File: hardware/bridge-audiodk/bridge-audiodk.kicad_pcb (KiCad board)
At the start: 6 copper layers, 5 parts, among them J1 Conn_01x08_Pin, J2 Conn_01x06_Pin, J3 Conn_01x08_Pin, J4 Conn_01x08_Pin

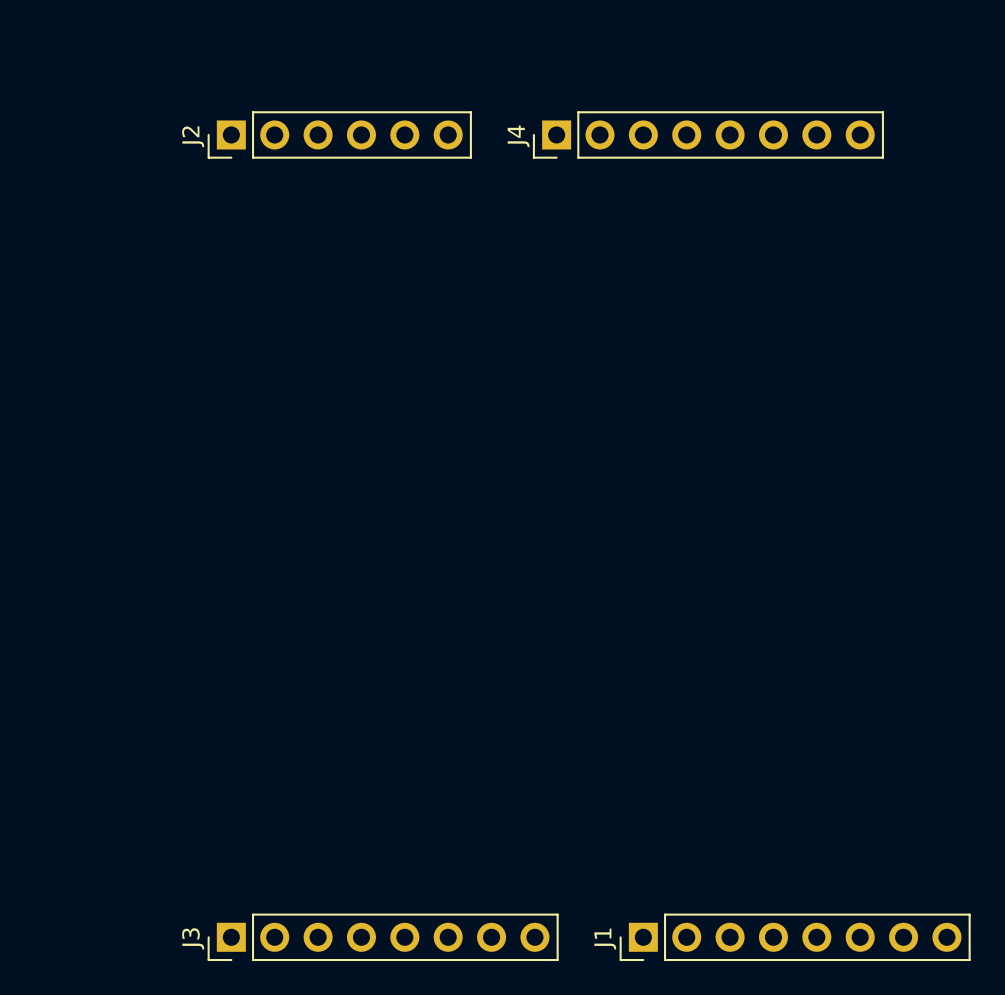
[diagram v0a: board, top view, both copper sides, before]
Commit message: Clean up repo for corporate migration, add release plan
- Remove KiCad autosave and backup files from tracking
- Update .gitignore: exclude .vscode/, .idea/, .mcp.json, KiCad autosaves
- Add docs/work/ with release plan and AI coder instructions
- Updated diagrams

Co-Authored-By: Claude Opus 4.6 <noreply@anthropic.com>
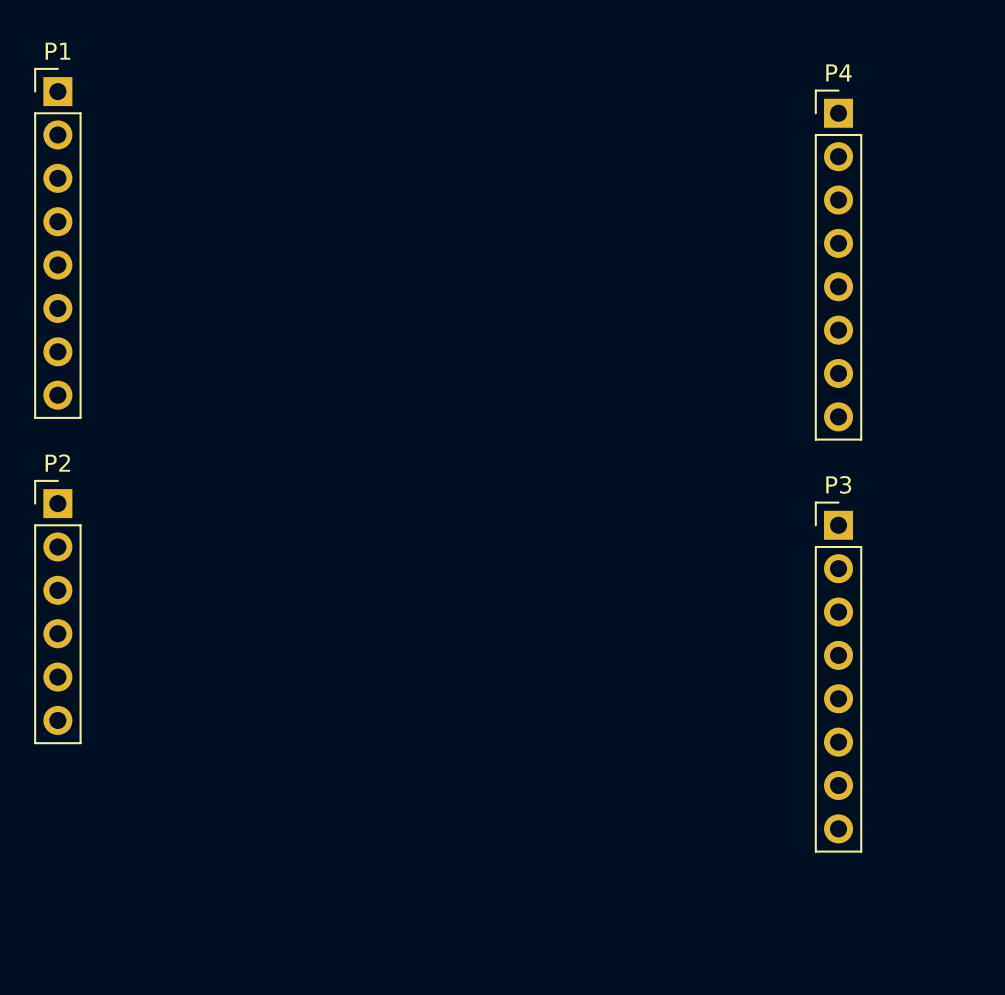
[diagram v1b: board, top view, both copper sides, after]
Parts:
- removed J1, J3, J4: Conn_01x08_Pin, Connector_PinHeader_2.54mm:PinHeader_1x08_P2.54mm_Vertical
- removed J2: Conn_01x06_Pin, Connector_PinHeader_2.54mm:PinHeader_1x06_P2.54mm_Vertical
- added P1: Conn_01x08_Pin, Connector_PinHeader_2.54mm:PinHeader_1x08_P2.54mm_Vertical, F.Cu at (124.9, 77.7)
- added P2: Conn_01x06_Pin, Connector_PinHeader_2.54mm:PinHeader_1x06_P2.54mm_Vertical, F.Cu at (124.9, 101.9)
- added P3: Conn_01x08_Pin, Connector_PinHeader_2.54mm:PinHeader_1x08_P2.54mm_Vertical, F.Cu at (170.6, 103.1)
- added P4: Conn_01x08_Pin, Connector_PinHeader_2.54mm:PinHeader_1x08_P2.54mm_Vertical, F.Cu at (170.6, 79.0)
